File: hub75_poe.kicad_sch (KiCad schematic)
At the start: 1 part

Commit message: Routing changes, pullups, etc
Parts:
- S1: Source (none) -> ANY

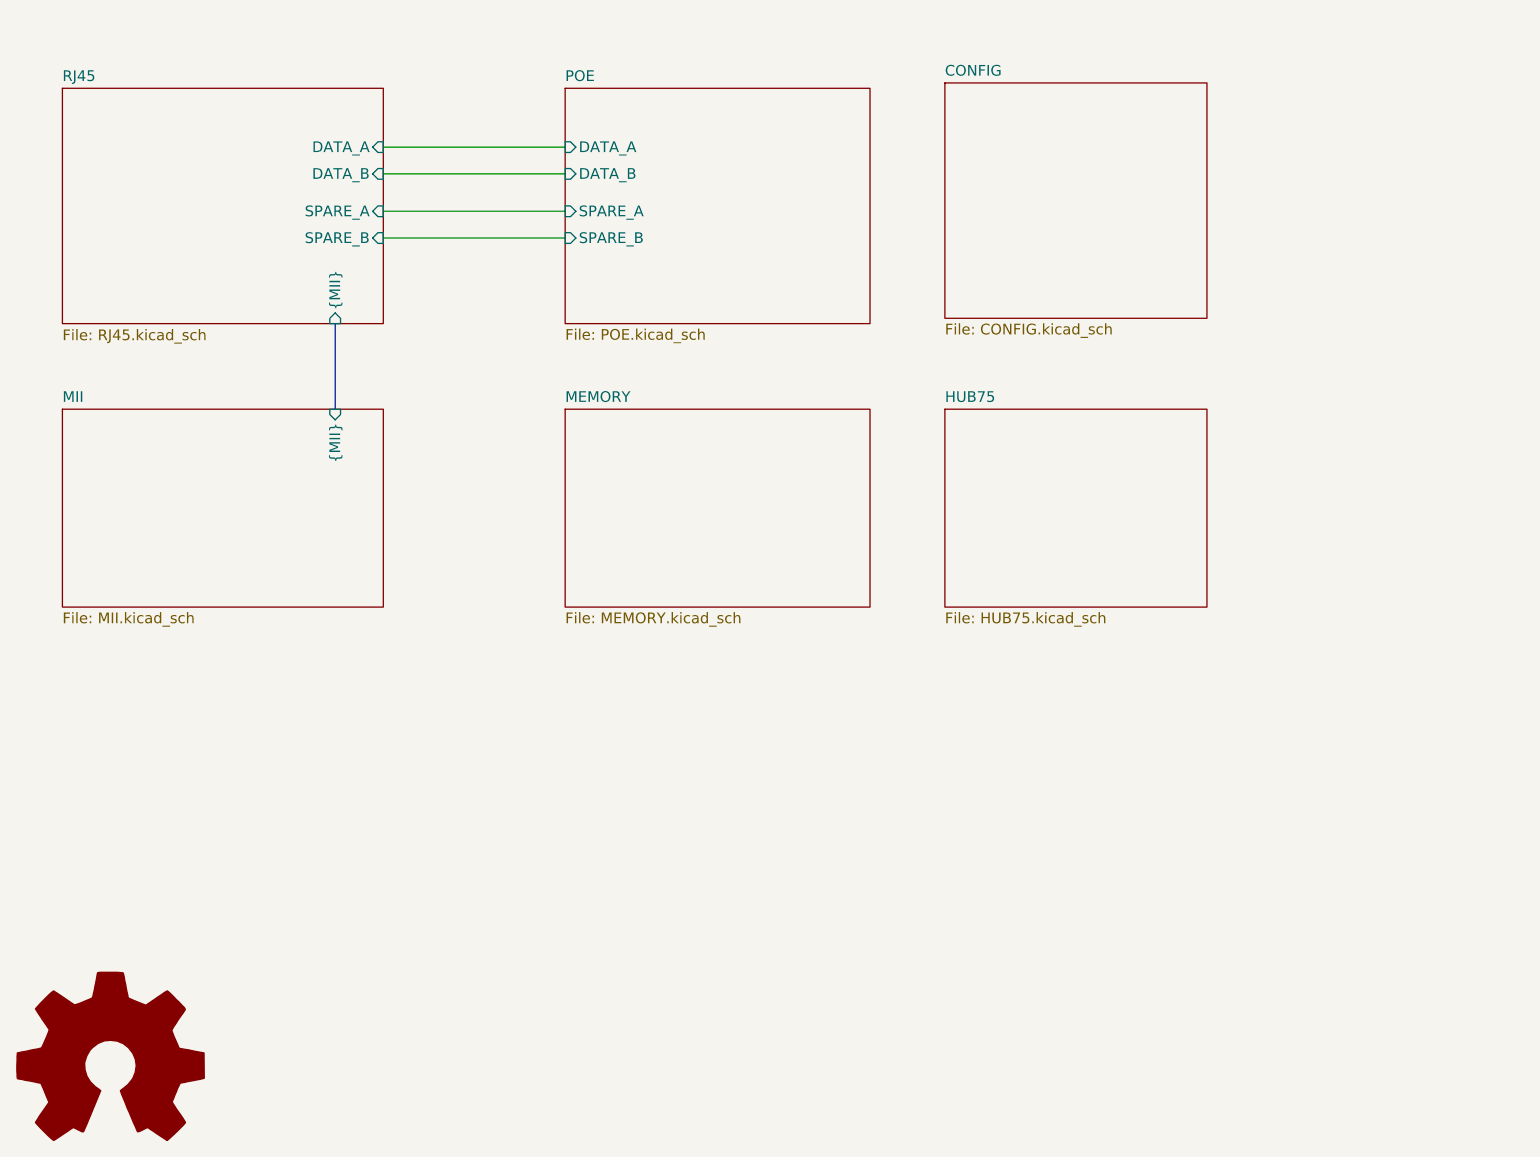
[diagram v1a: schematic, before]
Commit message: Routing cleanup, fix primary transformer
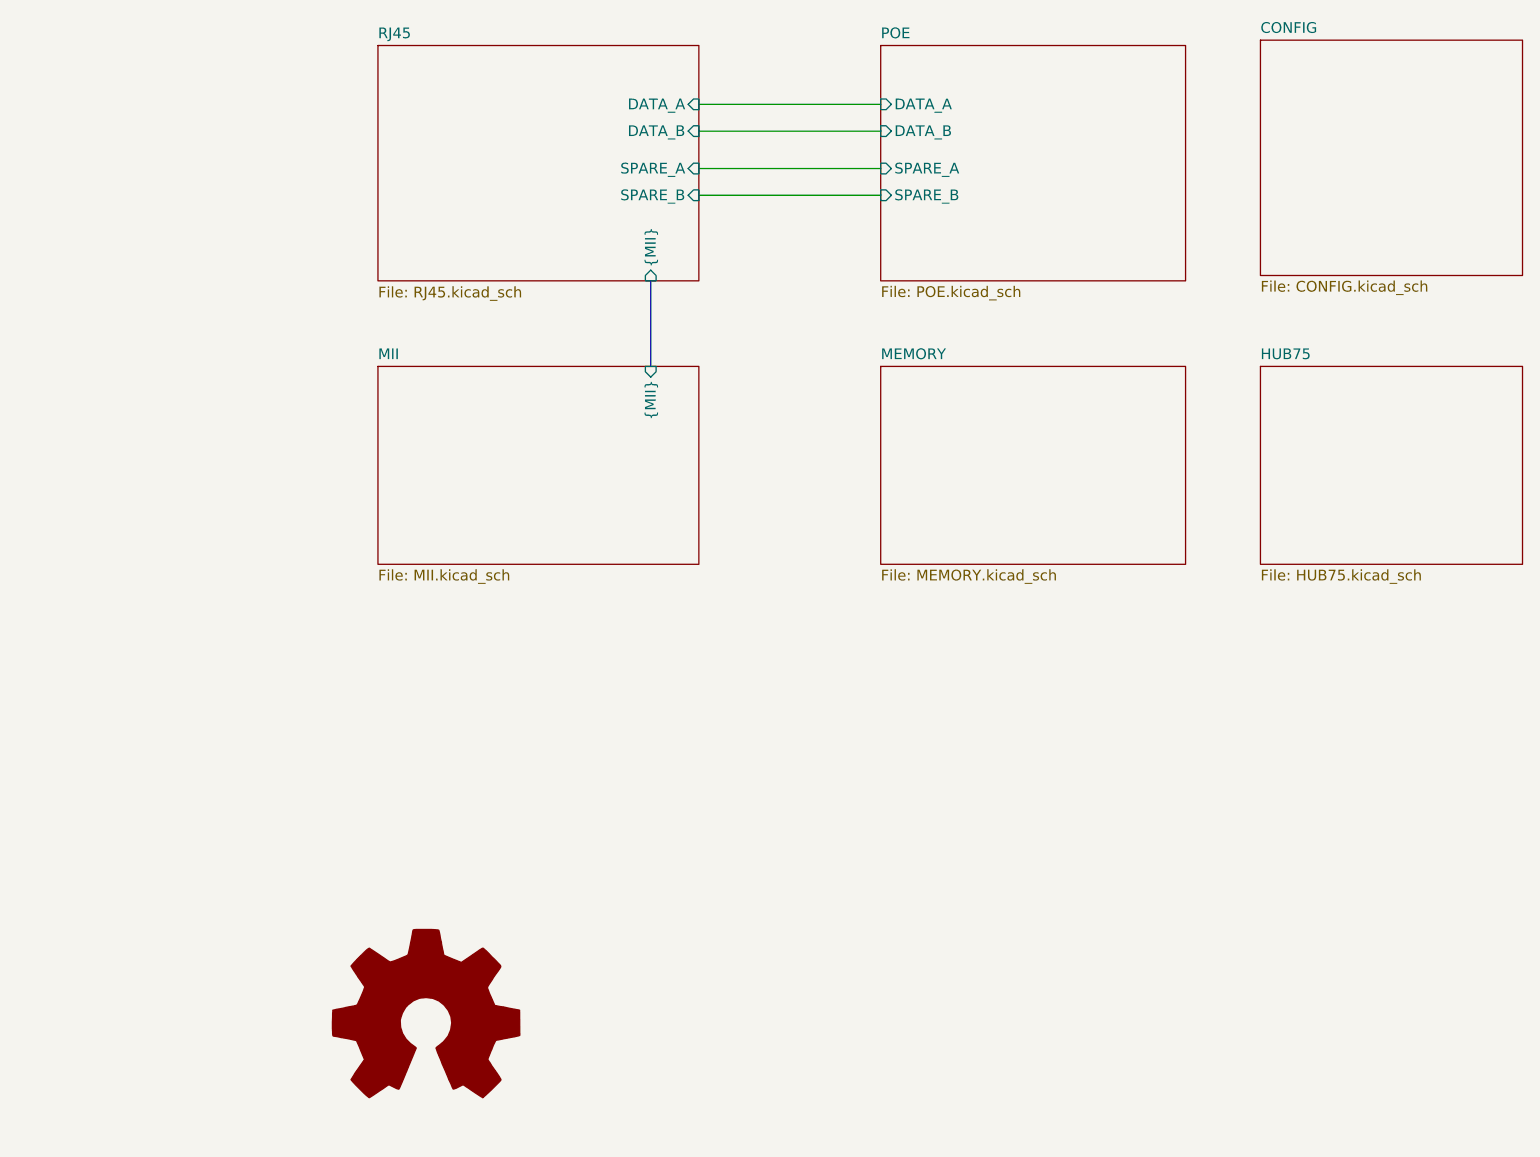
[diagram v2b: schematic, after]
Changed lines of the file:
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@@
   (page 1 7)
   (paper "A4")
-  (wire (pts (xy 67.31 52.705) (xy 88.9 52.705))
+  (title_block
+    (rev "TEST")
+  )
+  (wire (pts (xy 104.775 47.625) (xy 126.365 47.625))
     (stroke (width 0) (type solid) (color 0 0 0 0))
   )
-  (wire (pts (xy 67.31 55.88) (xy 88.9 55.88))
+  (wire (pts (xy 104.775 50.8) (xy 126.365 50.8))
     (stroke (width 0) (type solid) (color 0 0 0 0))
   )
-  (wire (pts (xy 67.31 60.325) (xy 88.9 60.325))
+  (wire (pts (xy 104.775 55.245) (xy 126.365 55.245))
     (stroke (width 0) (type solid) (color 0 0 0 0))
   )
-  (wire (pts (xy 67.31 63.5) (xy 88.9 63.5))
+  (wire (pts (xy 104.775 58.42) (xy 126.365 58.42))
     (stroke (width 0) (type solid) (color 0 0 0 0))
   )
-  (bus (pts (xy 61.595 73.66) (xy 61.595 83.82))
+  (bus (pts (xy 99.06 68.58) (xy 99.06 78.74))
     (stroke (width 0) (type solid) (color 0 0 0 0))
   )
-  (symbol (lib_id "Graphic:Logo_Open_Hardware_Large") (at 34.925 161.925 0) (unit 1)
-    (property "Reference" "S1" (id 0) (at 34.925 149.225 0)
+  (symbol (lib_id "Graphic:Logo_Open_Hardware_Large") (at 72.39 156.845 0) (unit 1)
+    (property "Reference" "S1" (id 0) (at 72.39 144.145 0)
       (effects (font (size 1.27 1.27)) hide)
     )
-    (property "Value" "Logo_Open_Hardware_Large" (id 1) (at 34.925 172.085 0)
+    (property "Value" "Logo_Open_Hardware_Large" (id 1) (at 72.39 167.005 0)
       (effects (font (size 1.27 1.27)) hide)
     )
-    (property "Footprint" "Symbol:OSHW-Symbol_6.7x6mm_SilkScreen" (id 2) (at 34.925 161.925 0)
+    (property "Footprint" "Symbol:OSHW-Symbol_6.7x6mm_SilkScreen" (id 2) (at 72.39 156.845 0)
       (effects (font (size 1.27 1.27)) hide)
     )
-    (property "Datasheet" "~" (id 3) (at 34.925 161.925 0)
+    (property "Datasheet" "~" (id 3) (at 72.39 156.845 0)
       (effects (font (size 1.27 1.27)) hide)
     )
-    (property "Source" "ANY" (id 4) (at 34.925 161.925 0)
+    (property "Source" "ANY" (id 4) (at 72.39 156.845 0)
       (effects (font (size 1.27 1.27)) hide)
     )
   )
-  (sheet (at 133.985 45.085) (size 31.115 27.94)
+  (sheet (at 171.45 40.005) (size 31.115 27.94)
     (stroke (width 0.152) (type solid) (color 132 0 132 1))
     (fill (color 255 255 255 0.0000))
-    (property "Sheet name" "CONFIG" (id 0) (at 133.985 44.3736 0)
+    (property "Sheet name" "CONFIG" (id 0) (at 171.45 39.2936 0)
       (effects (font (size 1.27 1.27)) (justify left bottom))
     )
-    (property "Sheet file" "CONFIG.kicad_sch" (id 1) (at 133.985 73.6094 0)
+    (property "Sheet file" "CONFIG.kicad_sch" (id 1) (at 171.45 68.5294 0)
       (effects (font (size 1.27 1.27)) (justify left top))
     )
   )
-  (sheet (at 133.985 83.82) (size 31.115 23.495)
+  (sheet (at 171.45 78.74) (size 31.115 23.495)
     (stroke (width 0.152) (type solid) (color 132 0 132 1))
     (fill (color 255 255 255 0.0000))
-    (property "Sheet name" "HUB75" (id 0) (at 133.985 83.1086 0)
+    (property "Sheet name" "HUB75" (id 0) (at 171.45 78.0286 0)
       (effects (font (size 1.27 1.27)) (justify left bottom))
     )
-    (property "Sheet file" "HUB75.kicad_sch" (id 1) (at 133.985 107.8994 0)
+    (property "Sheet file" "HUB75.kicad_sch" (id 1) (at 171.45 102.8194 0)
       (effects (font (size 1.27 1.27)) (justify left top))
     )
   )
-  (sheet (at 88.9 83.82) (size 36.195 23.495)
+  (sheet (at 126.365 78.74) (size 36.195 23.495)
     (stroke (width 0.152) (type solid) (color 132 0 132 1))
     (fill (color 255 255 255 0.0000))
-    (property "Sheet name" "MEMORY" (id 0) (at 88.9 83.1086 0)
+    (property "Sheet name" "MEMORY" (id 0) (at 126.365 78.0286 0)
       (effects (font (size 1.27 1.27)) (justify left bottom))
     )
-    (property "Sheet file" "MEMORY.kicad_sch" (id 1) (at 88.9 107.8994 0)
+    (property "Sheet file" "MEMORY.kicad_sch" (id 1) (at 126.365 102.8194 0)
       (effects (font (size 1.27 1.27)) (justify left top))
     )
   )
-  (sheet (at 29.21 83.82) (size 38.1 23.495)
+  (sheet (at 66.675 78.74) (size 38.1 23.495)
     (stroke (width 0.152) (type solid) (color 132 0 132 1))
     (fill (color 255 255 255 0.0000))
-    (property "Sheet name" "MII" (id 0) (at 29.21 83.1086 0)
+    (property "Sheet name" "MII" (id 0) (at 66.675 78.0286 0)
       (effects (font (size 1.27 1.27)) (justify left bottom))
     )
-    (property "Sheet file" "MII.kicad_sch" (id 1) (at 29.21 107.8994 0)
+    (property "Sheet file" "MII.kicad_sch" (id 1) (at 66.675 102.8194 0)
       (effects (font (size 1.27 1.27)) (justify left top))
     )
-    (pin "{MII}" input (at 61.595 83.82 90)
+    (pin "{MII}" input (at 99.06 78.74 90)
       (effects (font (size 1.27 1.27)) (justify right))
     )
   )
-  (sheet (at 88.9 45.72) (size 36.195 27.94)
+  (sheet (at 126.365 40.64) (size 36.195 27.94)
     (stroke (width 0.152) (type solid) (color 132 0 132 1))
     (fill (color 255 255 255 0.0000))
-    (property "Sheet name" "POE" (id 0) (at 88.9 45.0086 0)
+    (property "Sheet name" "POE" (id 0) (at 126.365 39.9286 0)
       (effects (font (size 1.27 1.27)) (justify left bottom))
     )
-    (property "Sheet file" "POE.kicad_sch" (id 1) (at 88.9 74.2444 0)
+    (property "Sheet file" "POE.kicad_sch" (id 1) (at 126.365 69.1644 0)
       (effects (font (size 1.27 1.27)) (justify left top))
     )
-    (pin "SPARE_A" input (at 88.9 60.325 180)
+    (pin "SPARE_A" input (at 126.365 55.245 180)
       (effects (font (size 1.27 1.27)) (justify left))
     )
-    (pin "SPARE_B" input (at 88.9 63.5 180)
+    (pin "SPARE_B" input (at 126.365 58.42 180)
       (effects (font (size 1.27 1.27)) (justify left))
     )
-    (pin "DATA_A" input (at 88.9 52.705 180)
+    (pin "DATA_A" input (at 126.365 47.625 180)
       (effects (font (size 1.27 1.27)) (justify left))
     )
-    (pin "DATA_B" input (at 88.9 55.88 180)
+    (pin "DATA_B" input (at 126.365 50.8 180)
       (effects (font (size 1.27 1.27)) (justify left))
     )
   )
-  (sheet (at 29.21 45.72) (size 38.1 27.94)
+  (sheet (at 66.675 40.64) (size 38.1 27.94)
     (stroke (width 0.152) (type solid) (color 132 0 132 1))
     (fill (color 255 255 255 0.0000))
-    (property "Sheet name" "RJ45" (id 0) (at 29.21 45.0086 0)
+    (property "Sheet name" "RJ45" (id 0) (at 66.675 39.9286 0)
       (effects (font (size 1.27 1.27)) (justify left bottom))
     )
-    (property "Sheet file" "RJ45.kicad_sch" (id 1) (at 29.21 74.295 0)
+    (property "Sheet file" "RJ45.kicad_sch" (id 1) (at 66.675 69.215 0)
       (effects (font (size 1.27 1.27)) (justify left top))
     )
-    (pin "DATA_A" input (at 67.31 52.705 0)
+    (pin "DATA_A" input (at 104.775 47.625 0)
       (effects (font (size 1.27 1.27)) (justify right))
     )
-    (pin "DATA_B" input (at 67.31 55.88 0)
+    (pin "DATA_B" input (at 104.775 50.8 0)
       (effects (font (size 1.27 1.27)) (justify right))
     )
-    (pin "SPARE_A" input (at 67.31 60.325 0)
+    (pin "SPARE_A" input (at 104.775 55.245 0)
       (effects (font (size 1.27 1.27)) (justify right))
     )
-    (pin "SPARE_B" input (at 67.31 63.5 0)
+    (pin "SPARE_B" input (at 104.775 58.42 0)
       (effects (font (size 1.27 1.27)) (justify right))
     )
-    (pin "{MII}" input (at 61.595 73.66 270)
+    (pin "{MII}" input (at 99.06 68.58 270)
       (effects (font (size 1.27 1.27)) (justify left))
     )
@@
       (reference "#PWR0175") (unit 1)
     )
+    (path "/15a5379a-5304-414f-b1d1-a2406f05f4a7/d6910270-aeae-4fc9-9a00-e4efb74fcf96"
+      (reference "#PWR0182") (unit 1)
+    )
     (path "/15a5379a-5304-414f-b1d1-a2406f05f4a7/8016e57f-0a5a-4054-99e9-fe1debb0312e"
       (reference "C1") (unit 1)
@@
       (reference "C26") (unit 1)
     )
+    (path "/e88c8a4a-9a9f-4489-82f2-72084410741f/21acf942-9a94-43db-a6e7-8e6d94ca8b16"
+      (reference "C39") (unit 1)
+    )
     (path "/e88c8a4a-9a9f-4489-82f2-72084410741f/73d6c9e7-5c14-4c04-9012-f6f01b5d7615"
       (reference "U2") (unit 2)
@@
       (reference "C33") (unit 1)
     )
+    (path "/1cd55ad1-6412-44cc-9669-b4acc6e6aaec/2eae118e-d312-465e-a85f-15ccdd6f232b"
+      (reference "C40") (unit 1)
+    )
     (path "/1cd55ad1-6412-44cc-9669-b4acc6e6aaec/fb2b86df-8c3a-41ac-b35d-5d6f30059ae9"
       (reference "D6") (unit 1)
@@
       (reference "R27") (unit 1)
     )
+    (path "/1cd55ad1-6412-44cc-9669-b4acc6e6aaec/f263c9bd-4813-423d-ae65-9711cf48a4ae"
+      (reference "R28") (unit 1)
+    )
     (path "/1cd55ad1-6412-44cc-9669-b4acc6e6aaec/50034c5b-de7e-42b7-b791-5e99f69b3cdc"
